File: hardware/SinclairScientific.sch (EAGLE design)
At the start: 92 parts, among them J1 JSTPH, J3 USB-MICRO, U2 SPX3819-3.3, U3 MCP73831T-2ACI/OT, U4 ATSAMD21G18, U5 W25Q128JVSO, X2 32.768

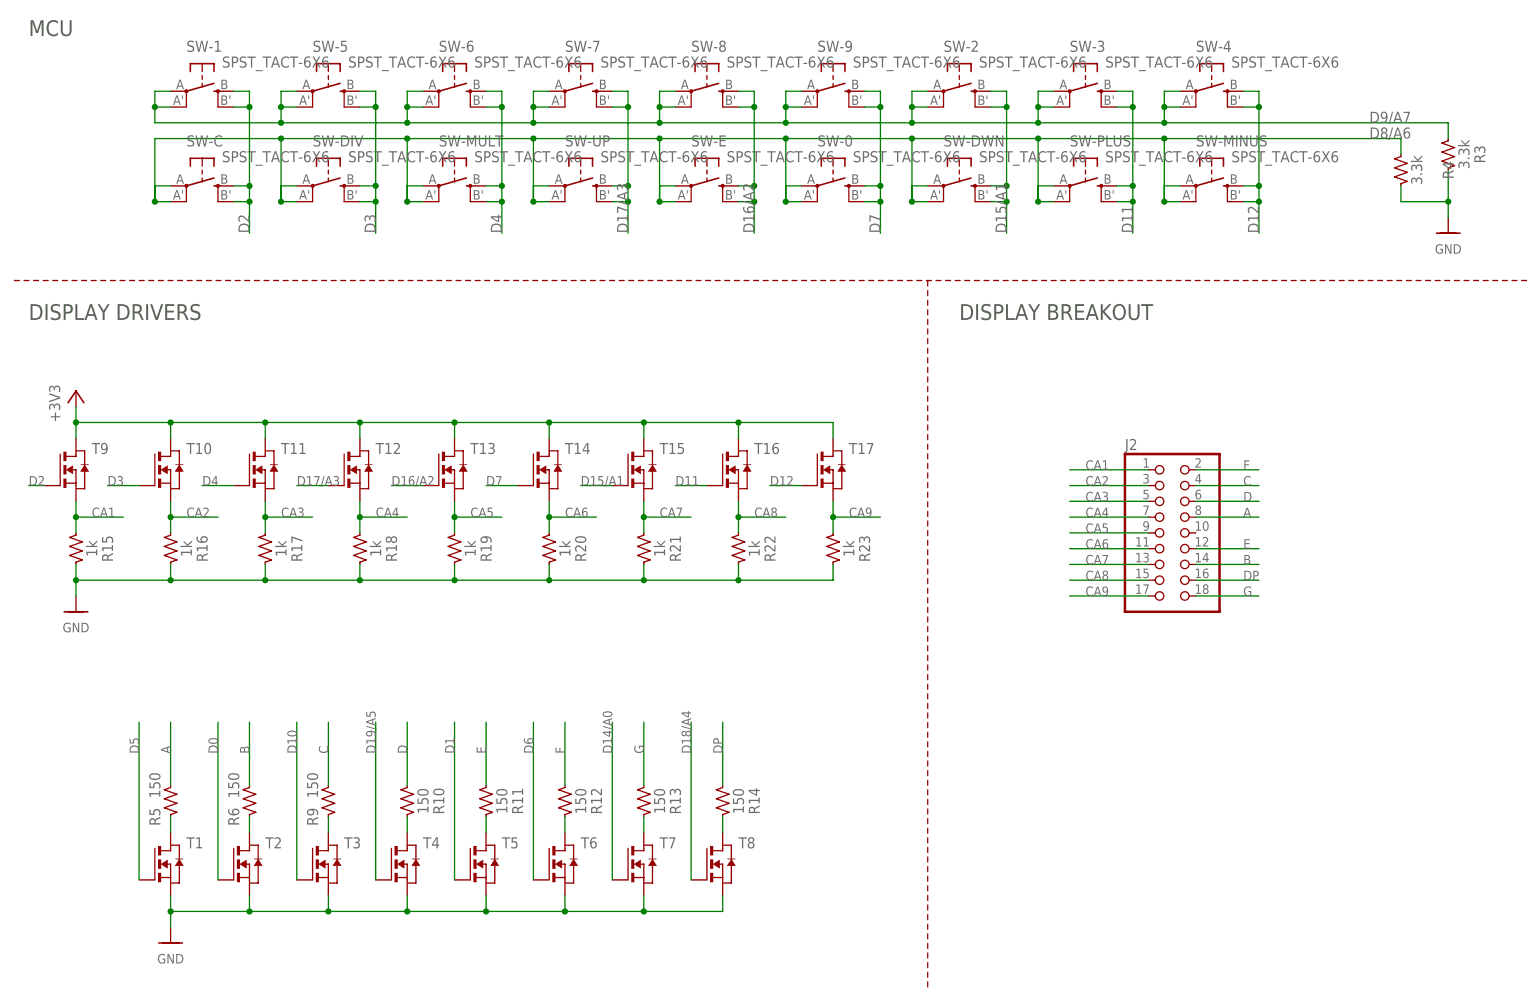
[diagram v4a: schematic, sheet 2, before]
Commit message: Converted local library to managed library. Fixed more hardware issues found from testing v1B prototype.
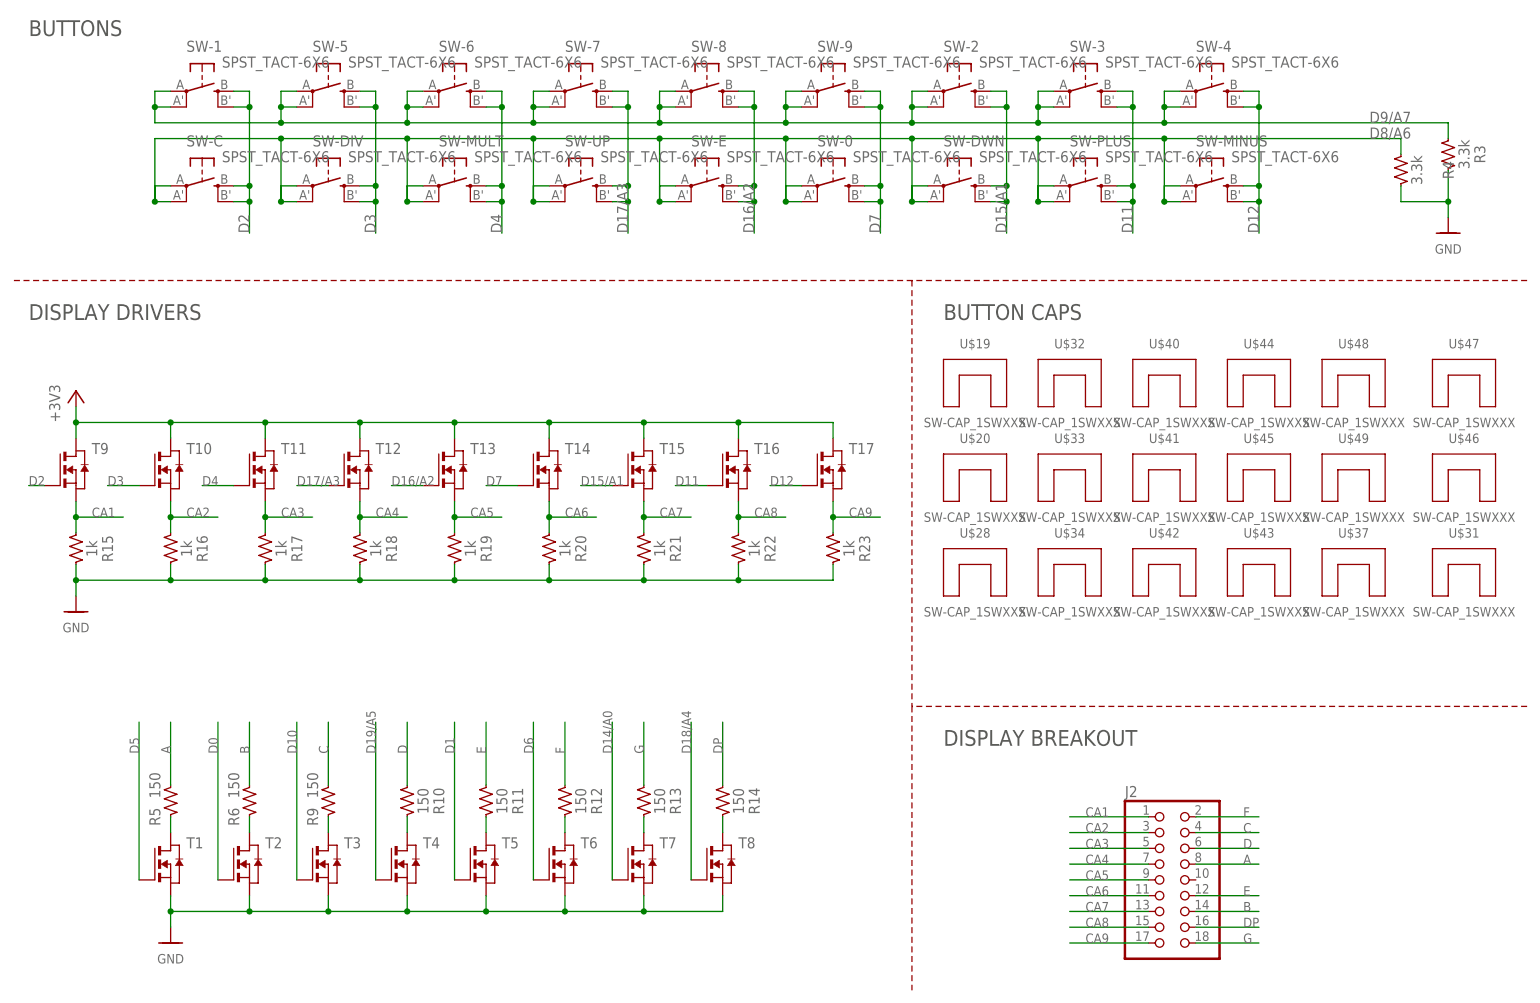
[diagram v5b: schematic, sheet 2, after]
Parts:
- added U$19, U$20, U$28, U$31, U$32, U$33, U$34, U$37, U$40, U$41, U$42, U$43, U$44, U$45, U$46, U$47, U$48, U$49: SW-CAP_1SWXXX, SinclairScientific:SW-CAP_1SWXXX
- U5: value W25Q128JVSO -> W25Q128JVWSON_6X5; device SinclairScientific:W25Q128JVSO -> SinclairScientific:W25Q128JVWSON_6X5
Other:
- note added: "BUTTON CAPS"
- note added: "BUTTONS"
- moved on the sheet: J2

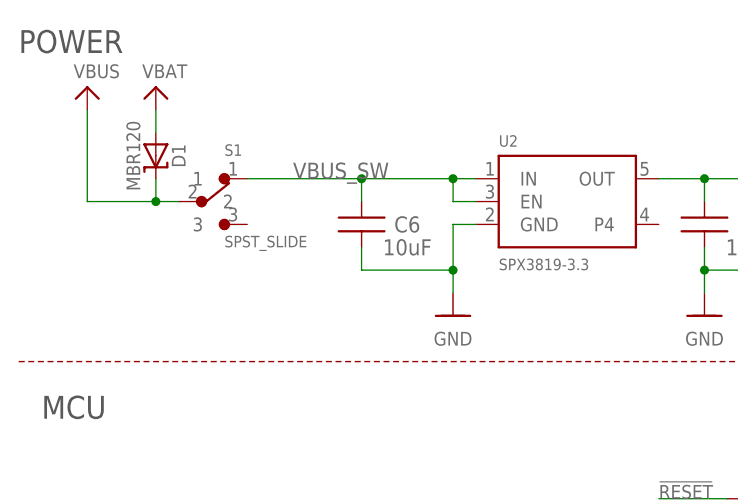
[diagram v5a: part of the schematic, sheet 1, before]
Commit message: Changed on/off switch to SMD type, fixed some DFM issues
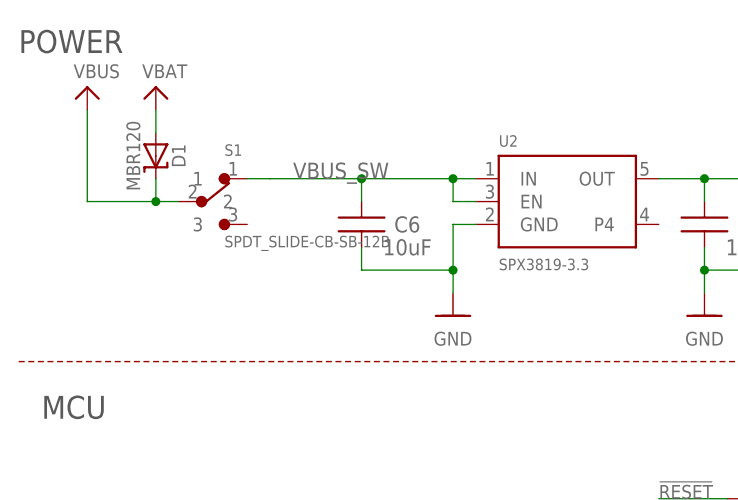
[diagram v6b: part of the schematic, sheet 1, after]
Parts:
- S1: value SPST_SLIDE -> SPDT_SLIDE-CB-SB-12B; device SinclairScientific:SPST_SLIDE -> SinclairScientific:SPDT_SLIDE-CB-SB-12B

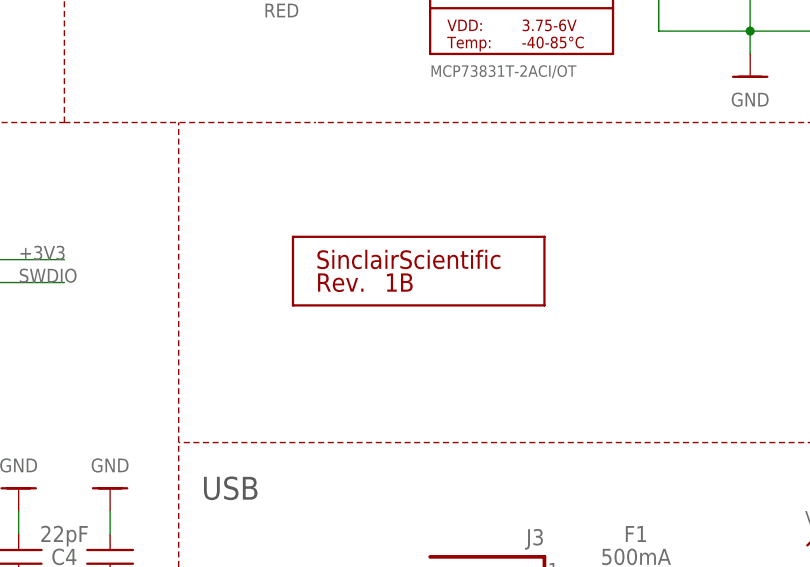
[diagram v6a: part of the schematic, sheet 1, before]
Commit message: Changed button spacing, finalized rev 1C layouts
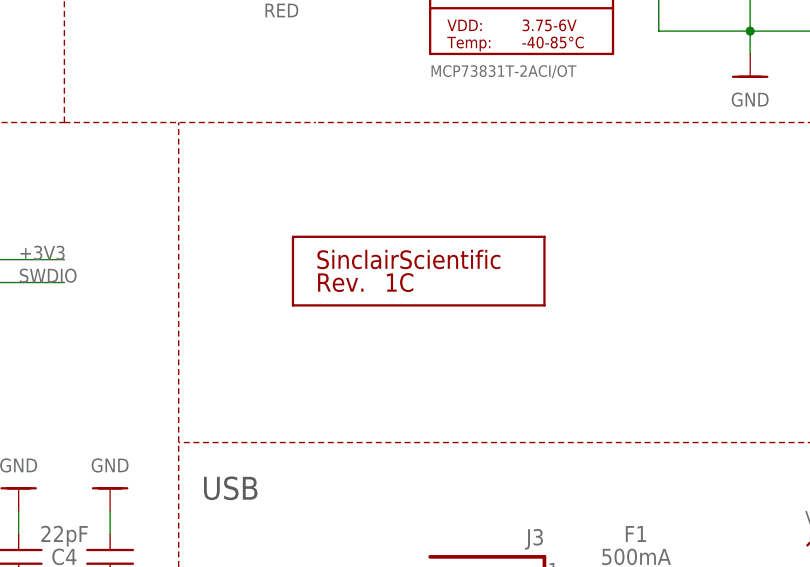
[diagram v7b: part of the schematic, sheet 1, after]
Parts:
- U$18: REV 1B -> 1C

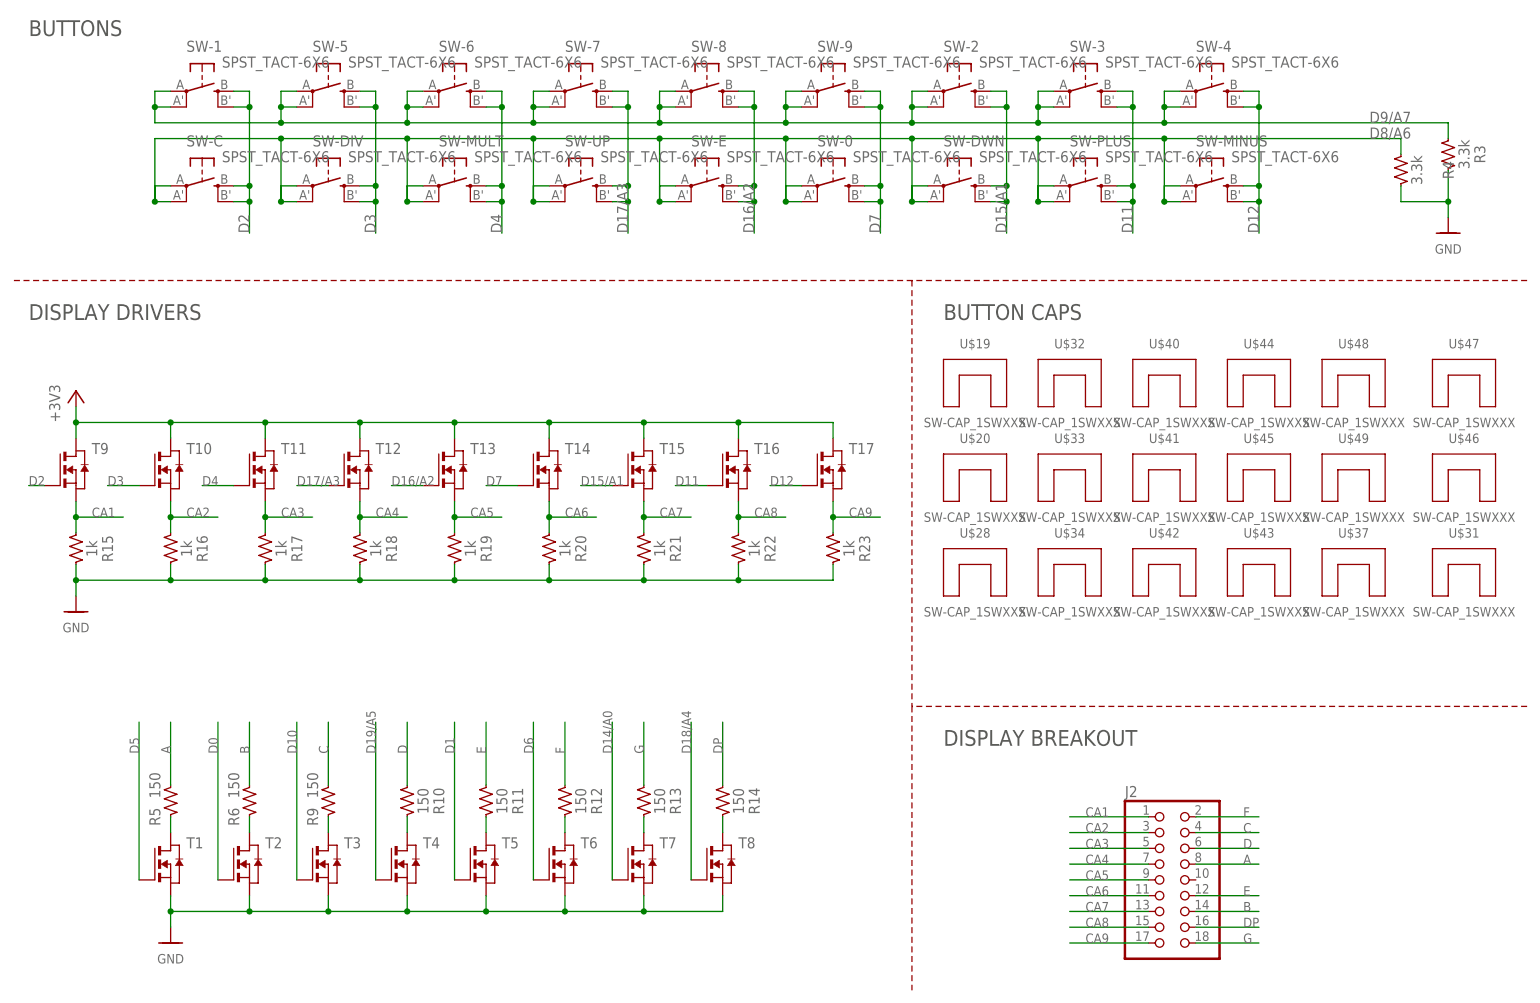
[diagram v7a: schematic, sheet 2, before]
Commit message: Updated BOM and added BOM attributes to schematic
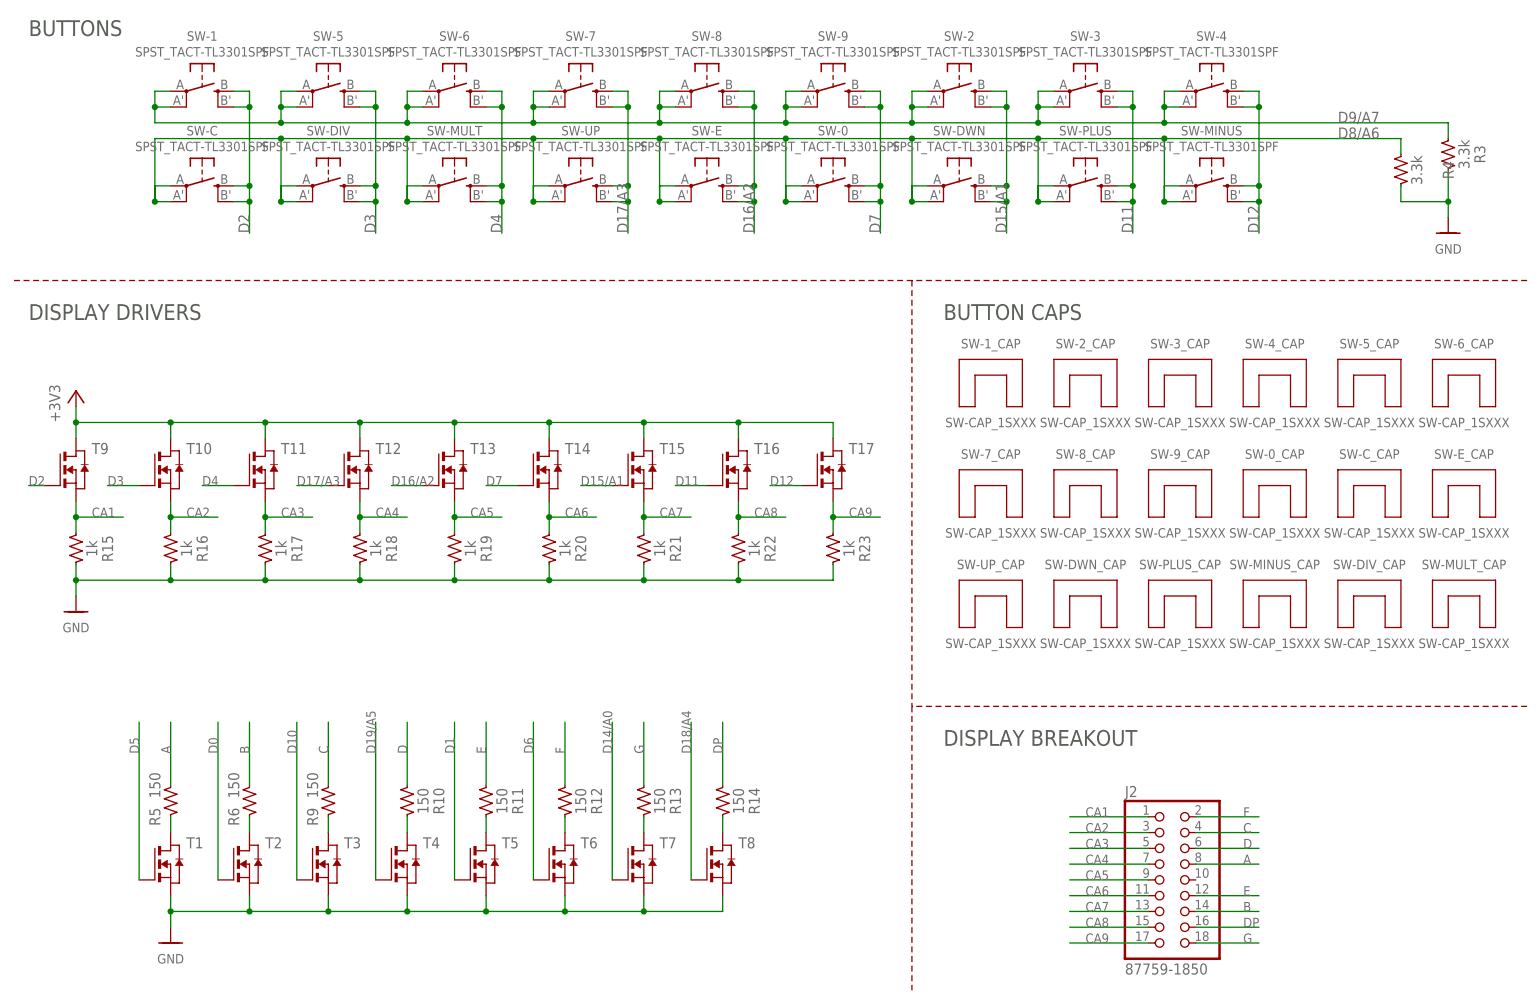
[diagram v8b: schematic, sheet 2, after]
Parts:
- removed U$19, U$20, U$28, U$31, U$32, U$33, U$34, U$37, U$40, U$41, U$42, U$43, U$44, U$45, U$46, U$47, U$48, U$49: SW-CAP_1SWXXX, SinclairScientific:SW-CAP_1SWXXX
- added SW-0_CAP, SW-1_CAP, SW-2_CAP, SW-3_CAP, SW-4_CAP, SW-5_CAP, SW-6_CAP, SW-7_CAP, SW-8_CAP, SW-9_CAP, SW-C_CAP, SW-DIV_CAP, SW-DWN_CAP, SW-E_CAP, SW-MINUS_CAP, SW-MULT_CAP, SW-PLUS_CAP, SW-UP_CAP: SW-CAP_1SXXX, SinclairScientific:SW-CAP_1SXXX
- C1, C12, C14, C7: value 1uF -> 1u; MFG (none) -> TDK Corporation; MPN (none) -> C1608X7R1C105M080AC; PN-DK (none) -> 445-5131-1-ND
- C10, C11, C9: MFG (none) -> AVX Corporation; MPN (none) -> 06035C104K4Z4A; PN-DK (none) -> 478-10679-1-ND
- C13, C3, C6, C8: value 10uF -> 10u; MFG (none) -> Murata Electronics North America; MPN (none) -> GRM21BR61C106KE15K; PN-DK (none) -> 490-6473-1-ND
- C15, C5: value 100nF -> 100n; MFG (none) -> AVX Corporation; MPN (none) -> 06035C104K4Z4A; PN-DK (none) -> 478-10679-1-ND
- C2, C4: value 22pF -> 22p; MFG (none) -> Murata Electronics North America; MPN (none) -> GQM1875C2E220JB12D; PN-DK (none) -> 490-16699-1-ND
- CHG: value RED -> GREEN-RA; MFG (none) -> Lite-On Inc.; MPN (none) -> LTST-S220KGKT; PN-DK (none) -> 160-1468-1-ND
- F1: MFG (none) -> Bel Fuse Inc.; MPN (none) -> 0ZCK0050FF2E; PN-DK (none) -> 507-1813-1-ND
- HB, L1: value RED -> GREEN; MFG (none) -> Lite-On Inc.; MPN (none) -> LTST-C170GKT; PN-DK (none) -> 160-1179-1-ND
- J1: MFG (none) -> JST Sales America Inc.; MPN (none) -> S2B-PH-SM4-TB(LF)(SN); PN-DK (none) -> 455-1749-1-ND
- J2: value (none) -> 87759-1850
- R1, R15, R16, R17, R18, R19, R2, R20, R21, R22, R23, R7: MFG (none) -> Yageo; MPN (none) -> RC0603FR-071KL; PN-DK (none) -> 311-1.00KHRCT-ND
- R10, R11, R12, R13, R14, R5, R6, R9: MFG (none) -> Yageo; MPN (none) -> RC0603FR-07150RL; PN-DK (none) -> 311-150HRCT-ND
- R3, R4, R8: MFG (none) -> Yageo; MPN (none) -> RC0603FR-073K3L; PN-DK (none) -> 311-3.30KHRCT-ND
- S1: MFG (none) -> Nidec Copal Electronics; MPN (none) -> CL-SB-12B-01T; PN-DK (none) -> 563-1318-1-ND
- SILK-QC: PRODUCT SinclairScientific -> Sinclair Scientific
- SW-0, SW-2, SW-3, SW-4, SW-5, SW-6, SW-7, SW-8, SW-9, SW-C, SW-DIV, SW-DWN, SW-E, SW-MINUS, SW-MULT, SW-PLUS, SW-UP: value SPST_TACT-6X6 -> SPST_TACT-TL3301SPF; device SinclairScientific:SPST_TACT-6X6 -> SinclairScientific:SPST_TACT-TL3301SPF
- SW-1: value SPST_TACT-6X6 -> SPST_TACT-TL3301SPF; device SinclairScientific:SPST_TACT-6X6 -> SinclairScientific:SPST_TACT-TL3301SPF; MFG (none) -> E-Switch; MPN (none) -> TL3301SPF260QG; PN-DK (none) -> EG1870CT-ND
- T1, T10, T11, T12, T13, T14, T15, T16, T17, T2, T3, T4, T5, T6, T7, T8: device SinclairScientific:NMOSSOT23 -> SinclairScientific:NMOSSOT23-FDV303N
- T9: device SinclairScientific:NMOSSOT23 -> SinclairScientific:NMOSSOT23-FDV303N; MFG (none) -> ON Semiconductor; MPN (none) -> FDV303N; PN-DK (none) -> FDV303NCT-ND
- TC1: PN-DK (none) -> TC2030-IDC-NL
- U4: MPN (none) -> ATSAMD21G18A-AUT; PN-DK (none) -> ATSAMD21G18A-AUTCT-ND
- U5: MFG (none) -> Winbond Electronics; MPN (none) -> W25Q128JVPIM; PN-DK (none) -> W25Q128JVPIMCT-ND
- X2: MFG (none) -> ECS Inc.; MPN (none) -> ECS-.327-12.5-34B-TR; PN-DK (none) -> XC1617CT-ND
- renumbered U$18 to SILK-QC, U$2 to FID2, U$35 to FID3, U$7 to FID1
